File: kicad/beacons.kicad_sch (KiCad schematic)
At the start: 23 parts, among them J1 USB_C_Receptacle_USB2.0_16P, J2 Conn_01x03, J3 Conn_01x18, U1 ESP32-S3-WROOM-1, U2 PN5321A3HN_C1xx, U3 74HC595

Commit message: Fix
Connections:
- net +3V3: now also U1.3 (EN)
- net VCC: no longer U1.3 (EN)

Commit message: More pcb work
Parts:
- removed U1: ESP32-S3-WROOM-1, RF_Module:ESP32-S3-WROOM-1, symbol RF_Module:ESP32-S3-WROOM-1
- added AE1: Antenna_Loop, symbol Device:Antenna_Loop
- added C1, C14, C2, C5: 100nF, Capacitor_SMD:C_0402_1005Metric, symbol Device:C
- added C10, C11: NFC_C2, Capacitor_SMD:C_0402_1005Metric, symbol Device:C
- added C12: .1uF, Capacitor_SMD:C_0402_1005Metric, symbol Device:C
- added C13: 4.7uF, Capacitor_SMD:C_0402_1005Metric, symbol Device:C
- added C15, C17: 47uF, Capacitor_SMD:C_0402_1005Metric, symbol Device:C
- added C16: 10nF, Capacitor_SMD:C_0402_1005Metric, symbol Device:C
- added C3, C4: 22pF, Capacitor_SMD:C_0402_1005Metric, symbol Device:C
- added C6, C7: 220pF, Capacitor_SMD:C_0402_1005Metric, symbol Device:C
- added C8, C9: NFC_C1, Capacitor_SMD:C_0402_1005Metric, symbol Device:C
- added IC1: AP7179DSKZ20-13, QFN50P350X350X80-21N-D, symbol AP7179DSKZ20-13:AP7179DSKZ20-13
- added J4: Conn_01x02, Connector_JST:JST_PH_B2B-PH-K_1x02_P2.00mm_Vertical, symbol Connector_Generic:Conn_01x02
- added L1, L2: 560nH, Inductor_SMD:L_0603_1608Metric, symbol Device:L
- added Q1: Q_NPN, symbol Device:Q_NPN
- added R10: 2k, Resistor_SMD:R_0402_1005Metric, symbol Device:R
- added R11, R9: 10k, Resistor_SMD:R_0402_1005Metric, symbol Device:R
- added R5: 1k, Resistor_SMD:R_0402_1005Metric, symbol Device:R
- added R6: 2.7k, Resistor_SMD:R_0402_1005Metric, symbol Device:R
- added R7, R8: NFC_RQ, Resistor_SMD:R_0402_1005Metric, symbol Device:R
- added SW1: SW_Push, symbol Switch:SW_Push
- added SW2: SW_SPST, symbol Switch:SW_SPST
- added U1: ESP32-S3-WROOM-1, PCM_Espressif:ESP32-S3-WROOM-1, symbol PCM_Espressif:ESP32-S3-WROOM-1
- added U4: MAX17048G+T10, footprints:21-0168E_T822-3_MXM, symbol battmon:MAX17048G+T10
- added U5: MCP73831-2-OT, Package_TO_SOT_SMD:SOT-23-5, symbol Battery_Management:MCP73831-2-OT
- added Y1: Crystal 27.12MHz, symbol Device:Crystal
- D1: footprint (none) -> Diode_SMD:D_SOD-323
- J1: footprint (none) -> Connector_USB:USB_C_Receptacle_GCT_USB4105-xx-A_16P_TopMnt_Horizontal
- J2: footprint (none) -> Connector_JST:JST_PH_B3B-PH-K_1x03_P2.00mm_Vertical
- LED1, LED2: footprint SC10-11EWA_KNB -> footprints:SC10-11EWA_KNB
- R1, R2: value R -> 330; footprint (none) -> Resistor_SMD:R_0402_1005Metric
- R3, R4: footprint (none) -> Resistor_SMD:R_0402_1005Metric
- U3: footprint (none) -> Package_SO:SSOP-16_5.3x6.2mm_P0.65mm
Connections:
- net I2C_SDA is gone; now on net I2C_SCL: J3.14 (Pin_14)
- net +3V3: now also U2.17 (I1), U2.23 (PVDD), U2.39 (DVDD), U2.40 (VBAT), U2.5 (TVDD), U2.8 (AVDD), C1.2, C12.1, C2.2, R9.2, U1.2 (3V3), U1.3 (EN), U4.3 (VDD)
- net +5V: now also C14.2, C17.2, IC1.1 (OUT_1), Q1.C, U5.4 (V_{DD})
- net GND: now also U2.1 (DVSS), U2.11 (AVSS), U2.16 (I0), U2.18 (TESTEN), U2.3 (TVSS1), U2.41 (AVSS), U2.7 (TVSS2), C1.1, C10.2, C11.1, C12.2, C13.1, C14.1, C15.1, C16.1, C17.1, C2.1, C3.1, C4.2, C5.2, C6.1, C7.1, IC1.18 (GND_2), IC1.8 (GND_1), J4.2 (Pin_2), R10.1, SW1.2, U1.1 (GND), U1.16 (GPIO46), U1.40 (GND), U1.41 (GND), U4.1 (CTG), U4.4 (GND), U4.9 (EPAD), U5.2 (V_{SS})
- net I2C_SCL: now also U2.27 (NSS/P50_SCL/HSU_RX), U2.28 (MOSI/SDA/HSU_TX), U4.6 (QSTRT), U4.7 (SCL), U4.8 (SDA)
- net LED_SPI: now also R11.1; no longer D2.4 (DIN)
- net USB_NEG: now also U1.13 (GPIO19/U1RTS/ADC2_CH8/CLK_OUT2/USB_D-)
- net USB_POS: now also U1.14 (GPIO20/U1CTS/ADC2_CH9/CLK_OUT1/USB_D+)
- net at U2.10 (RX): now also R5.1, R6.1
- net at U2.14 (OSCIN): now also C3.2, Y1.1
- net at U2.15 (OSCOUT): now also C4.1, Y1.2
- net NFC_RESET: now reaches U2.38 (~{RSTPD})
- net at U2.4 (TX1): now also L1.1
- net at U2.6 (TX2): now also L2.1
- net at U2.9 (VMID): now also C5.1, R5.2
- new net: C16.2, IC1.13 (NR/SS)
- new net: R10.2, U5.5 (PROG)
- new net: Q1.B, R11.2
- new net: C7.2, C9.1, L2.2
- new net: C10.1, C9.2, R8.1
- new net: C6.2, C8.1, L1.2, R6.2
- new net: C11.2, C8.2, R7.1
- new net: AE1.1, R7.2
- new net: AE1.2, R8.2
- new net CELL_POS: C13.2, J4.1 (Pin_1), SW2.1 (A), U4.2 (CELL), U5.3 (V_{BAT})
- new net CHARGE_STAT: U5.1 (STAT)
- new net ESP_BOOT: R9.1, SW1.1, U1.27 (GPIO0/BOOT)
- new net LED_SPI_5V: D2.4 (DIN), Q1.E
- new net REG_POS: C15.2, IC1.14 (EN), IC1.15 (IN_1), SW2.2 (B)
- no-connect marks 8 -> 37
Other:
- moved on the sheet: D1, D10, D11, D2, D3, D4, D5, D6, D7, D8, D9, J1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

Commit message: Tons of stuff
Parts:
- removed U2: PN5321A3HN_C1xx, Package_DFN_QFN:HVQFN-40-1EP_6x6mm_P0.5mm_EP4.1x4.1mm, symbol RF_NFC:PN5321A3HN_C1xx
- added C18, C20: 10nF, symbol Device:C
- added C19, C21: 47uF, Capacitor_SMD:C_0402_1005Metric, symbol Device:C
- added C22: 10nF, Capacitor_SMD:C_0402_1005Metric, symbol Device:C
- added C23, C24: C_RX, symbol Device:C
- added C25, C27: C_0, symbol Device:C
- added C29, C31: C_1, symbol Device:C
- added C33, C34: C_2, symbol Device:C
- added IC2: AP7179DSKZ20-13, QFN50P350X350X80-21N-D, symbol AP7179DSKZ20-13:AP7179DSKZ20-13
- added IC3: PN7160A1HN_C100E, QFN50P600X600X100-41N-D, symbol PN7160A1HN_C100E:PN7160A1HN_C100E
- added R12: 12.4k, symbol Device:R
- added R13: 2.37k, symbol Device:R
- added R14: 11.8k, symbol Device:R
- added R15: 3.74k, symbol Device:R
- AE1: footprint (none) -> footprints:NFC
- C1: footprint Capacitor_SMD:C_0402_1005Metric -> (none)
- C10: value NFC_C2 -> 100nF; footprint Capacitor_SMD:C_0402_1005Metric -> (none)
- C11: value NFC_C2 -> 4.7uF; footprint Capacitor_SMD:C_0402_1005Metric -> (none)
- C3, C4: value 22pF -> 2.2uF; footprint Capacitor_SMD:C_0402_1005Metric -> (none)
- C5: value 100nF -> 22pF; footprint Capacitor_SMD:C_0402_1005Metric -> (none)
- C6: value 220pF -> 22pF; footprint Capacitor_SMD:C_0402_1005Metric -> (none)
- C7: value 220pF -> 2.2uF; footprint Capacitor_SMD:C_0402_1005Metric -> (none)
- C8: value NFC_C1 -> 2.2uF; footprint Capacitor_SMD:C_0402_1005Metric -> (none)
- C9: value NFC_C1 -> 4.7uF; footprint Capacitor_SMD:C_0402_1005Metric -> (none)
- L1, L2: value 560nH -> L_0; footprint Inductor_SMD:L_0603_1608Metric -> (none)
- R5: value 1k -> R_RX; footprint Resistor_SMD:R_0402_1005Metric -> (none)
- R6: value 2.7k -> R_RX; footprint Resistor_SMD:R_0402_1005Metric -> (none)
- R7, R8: value NFC_RQ -> R_Q; footprint Resistor_SMD:R_0402_1005Metric -> (none)
- SW2: footprint (none) -> Connector_JST:JST_PH_B2B-PH-K_1x02_P2.00mm_Vertical
- Y1: value Crystal 27.12MHz -> 27.12MHz Crystal
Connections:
- net +3V3: now also C19.2, C20.1, IC2.1 (OUT_1), IC3.10 (VEN), R14.2; no longer C1.2
- net +5V: now also C18.1, R12.2
- net GND: now also C1.2, C11.2, C3.2, C5.1, C7.2, C8.2, C9.2, C19.1, C21.1, C22.1, C25.2, C27.1, C33.2, C34.1, IC2.18 (GND_2), IC2.8 (GND_1), IC3.1 (I2C_ADR0/SPI_NSS), IC3.20 (VSS(TX)), IC3.3 (I2C_ADR1/SPI_MOSI), IC3.4 (VSS_1), IC3.41 (VSS_2), IC3.9 (VSS(A)), R13.2, R15.2; no longer C1.1, C11.1, C3.1, C5.2, C7.1
- net I2C_SCL: now also IC3.7 (I2C_SCL/SPI_SCK); no longer J3.14 (Pin_14), U4.6 (QSTRT), U4.8 (SDA)
- net NFC_IRQ: now also IC3.8 (IRQ)
- net REG_POS: now also C21.2, IC2.14 (EN), IC2.15 (IN_1)
- net at R6.1: now also C24.2; no longer R5.1
- net at R5.2: now also L1.2, C25.1, C29.1; no longer C5.1
- net at Y1.1: now also C6.2, IC3.29 (XTAL2); no longer C3.2
- net at Y1.2: now also C5.2, IC3.30 (NFC_CLK_XTAL1); no longer C4.1
- net NFC_TX1: now reaches L1.1
- net NFC_TX1: now also IC3.21 (TX1)
- net NFC_TX2: now reaches L2.1
- net NFC_TX2: now also IC3.19 (TX2)
- net at IC1.3 (FB): now also C18.2, R12.1, R13.1
- new net: C20.2, IC2.3 (FB), R14.1, R15.1
- new net: C29.2, C33.1, R7.1
- new net: C10.1, C9.1, IC3.12 (VBAT2), IC3.28 (VBAT)
- new net: C27.2, C31.1, L2.2, R6.2
- new net: C3.1, C4.1, IC3.14 (VDD(TX)), IC3.18 (TVDD_IN), IC3.22 (VDD_IN2)
- new net: C11.1, IC3.13 (VDD(UP))
- new net: C7.1, C8.1, IC3.26 (VDD(A)), IC3.27 (VDD_2), IC3.31 (VDD(D)), IC3.6 (VDD_1)
- new net: C22.2, IC2.13 (NR/SS)
- new net: C23.2, R5.1
- new net: C31.2, C34.2, R8.1
- new net: C1.1, IC3.17 (VDD(VMID))
- new net I2C_SDA: IC3.5 (I2C_SDA/SPI_MISO), J3.14 (Pin_14), U4.8 (SDA)
- new net NFC_FWUD: IC3.2 (DWL_REQ)
- new net NFC_RXN: C24.1, IC3.15 (RXN)
- new net NFC_RXP: C23.1, IC3.16 (RXP)
- no-connect marks 37 -> 48
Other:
- moved on the sheet: C17, J3

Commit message: Routing and RF
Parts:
- removed AE1: Antenna_Loop, footprints:NFC, symbol Device:Antenna_Loop
- removed C1, C10: 100nF, symbol Device:C
- removed C11, C9: 4.7uF, symbol Device:C
- removed C23, C24: C_RX, symbol Device:C
- removed C25, C27: C_0, symbol Device:C
- removed C29, C31: C_1, symbol Device:C
- removed C3, C4, C7, C8: 2.2uF, symbol Device:C
- removed C33, C34: C_2, symbol Device:C
- removed C5, C6: 22pF, symbol Device:C
- removed D10, D11: WS2812B, LED_SMD:LED_WS2812B_PLCC4_5.0x5.0mm_P3.2mm, symbol LED:WS2812B
- removed IC3: PN7160A1HN_C100E, QFN50P600X600X100-41N-D, symbol PN7160A1HN_C100E:PN7160A1HN_C100E
- removed L1, L2: L_0, symbol Device:L
- removed R5, R6: R_RX, symbol Device:R
- removed R7, R8: R_Q, symbol Device:R
- removed Y1: 27.12MHz Crystal, symbol Device:Crystal
- C18, C20: footprint (none) -> Capacitor_SMD:C_0402_1005Metric
- IC1, IC2: footprint QFN50P350X350X80-21N-D -> footprints:QFN50P350X350X80-21N-D
- J4, SW2: footprint Connector_JST:JST_PH_B2B-PH-K_1x02_P2.00mm_Vertical -> Connector_AMASS:AMASS_XT30UPB-M_1x02_P5.0mm_Vertical
- Q1: footprint (none) -> Package_TO_SOT_SMD:SOT-23; symbol Device:Q_NPN -> Transistor_BJT:MMBT3904
- R12, R13, R14, R15: footprint (none) -> Resistor_SMD:R_0402_1005Metric
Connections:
- net VCC is gone; now on net +3V3: U3.10 (~{SRCLR})
- net +5V: now also Q1.3 (C); no longer C14.2, D1.1 (K), Q1.C, U5.4 (V_{DD})
- net GND: now also U4.6 (QSTRT)
- net LED_PEAK: now also D9.2 (DOUT)
- net LED_SPI_5V: now also Q1.2 (E); no longer Q1.E
- net at R11.2: now also Q1.1 (B); no longer Q1.B
- net at LED2.14: now also LED2.3, LED2.6, R2.1
- net at LED1.6, R1.1: now also LED1.14, LED1.3
- new net USB_VBUS: C14.2, D1.1 (K), U5.4 (V_{DD})
- no-connect marks 48 -> 38
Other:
- added sheet NFC (nfc.kicad_sch)
- moved on the sheet: D1, J1, J3, LED1, LED2, R1, R11, R2, R3, R4, U3

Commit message: First revision
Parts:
- added C28, C30: .1uF, Capacitor_SMD:C_0402_1005Metric, symbol Device:C
- added C32: 22uF, Capacitor_SMD:C_0402_1005Metric, symbol Device:C
- added SW2: SW_Push, footprints:SMT_4.2X3.2_, symbol SKRPACE010:SKRPACE010
- J3: footprint (none) -> footprints:DisplayConnector
- SW1: footprint (none) -> footprints:SMT_4.2X3.2_; symbol Switch:SW_Push -> SKRPACE010:SKRPACE010; Arrow Part Number (none) -> SKRPACE010; Arrow Price/Stock (none) -> https://www.arrow.com/en/products/skrpace010/alps-electric; Manufacturer_Name (none) -> ALPS Electric; Manufacturer_Part_Number (none) -> SKRPACE010; Mouser Part Number (none) -> 688-SKRPACE010; Mouser Price/Stock (none) -> https://www.mouser.co.uk/ProductDetail/Alps-Alpine/SKRPACE0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
- renumbered SW2 to SW3
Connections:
- net +3V3: now also R9.1, C32.2; no longer R9.2, U1.3 (EN)
- net CHARGE_STAT: now also U1.12 (GPIO8/TOUCH8/ADC1_CH7/SUBSPICS1)
- net DISP_CS: now also U1.36 (U0RXD/GPIO44/CLK_OUT2)
- net DISP_RESET: now also U1.21 (GPIO13/TOUCH13/ADC2_CH2/FSPIQ/FSPIIO7/SUBSPIQ)
- net ESP_BOOT: now also SW1.2, C28.1; no longer R9.1
- net GND: now also SW1.3, SW1.4, C28.2, C30.2, C32.1, SW2.3, SW2.4; no longer SW1.2
- net I2C_SCL: now also U1.19 (GPIO11/TOUCH11/ADC2_CH0/FSPID/FSPIIO5/SUBSPID)
- net I2C_SDA: now also U1.18 (GPIO10/TOUCH10/ADC1_CH9/FSPICS0/FSPIIO4/SUBSPICS0)
- net LED_SPI: now also U1.37 (U0TXD/GPIO43/CLK_OUT1)
- net NFC_FWUD: now also U1.15 (GPIO3/TOUCH3/ADC1_CH2)
- net NFC_IRQ: now also U1.11 (GPIO18/U1RXD/ADC2_CH7/CLK_OUT3)
- net SPI_CLK: now also U1.26 (GPIO45)
- net SPI_DATA0: now also U1.25 (GPIO48/SPICLK_N/SUBSPICLK_N_DIFF)
- net SPI_DATA1: now also U1.24 (GPIO47/SPICLK_P/SUBSPICLK_P_DIFF)
- net SPI_DATA2: now also U1.23 (GPIO21)
- net SPI_DATA3: now also U1.22 (GPIO14/TOUCH14/ADC2_CH3/FSPIWP/FSPIDQS/SUBSPIWP)
- net SR_CS: now also U1.4 (GPIO4/TOUCH4/ADC1_CH3)
- net SS0: now also U1.9 (GPIO16/U0CTS/ADC2_CH5/XTAL_32K_N)
- net SS1: now also U1.10 (GPIO17/U1TXD/ADC2_CH6)
- net TOUCH_IRQ: now also U1.17 (GPIO9/TOUCH9/ADC1_CH8/FSPIHD/SUBSPIHD)
- net TOUCH_RESET: now also U1.20 (GPIO12/TOUCH12/ADC2_CH1/FSPICLK/FSPIIO6/SUBSPICLK)
- new net ESP_EN: C30.1, R9.2, SW2.1, SW2.2, U1.3 (EN)
- no-connect marks 38 -> 45

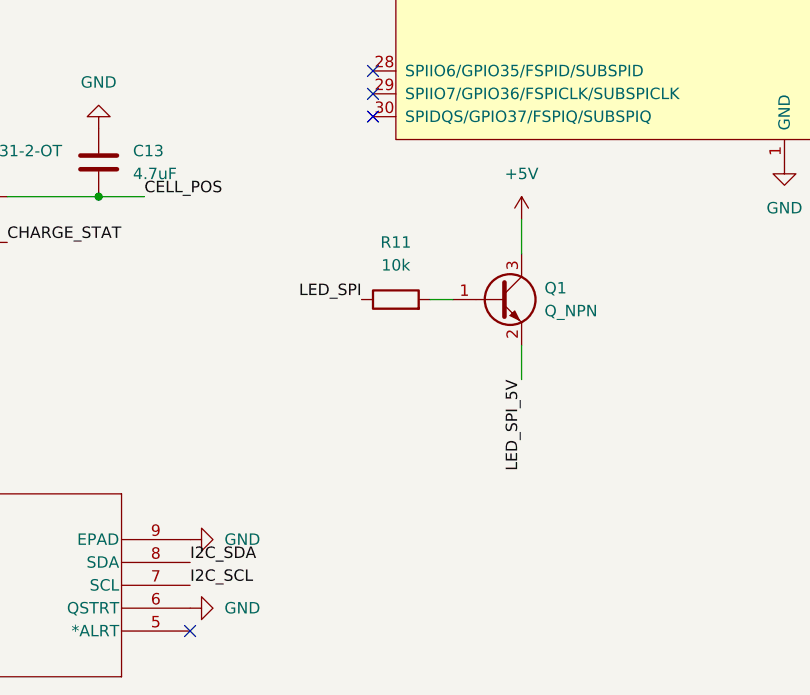
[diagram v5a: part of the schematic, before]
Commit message: Added level shifter
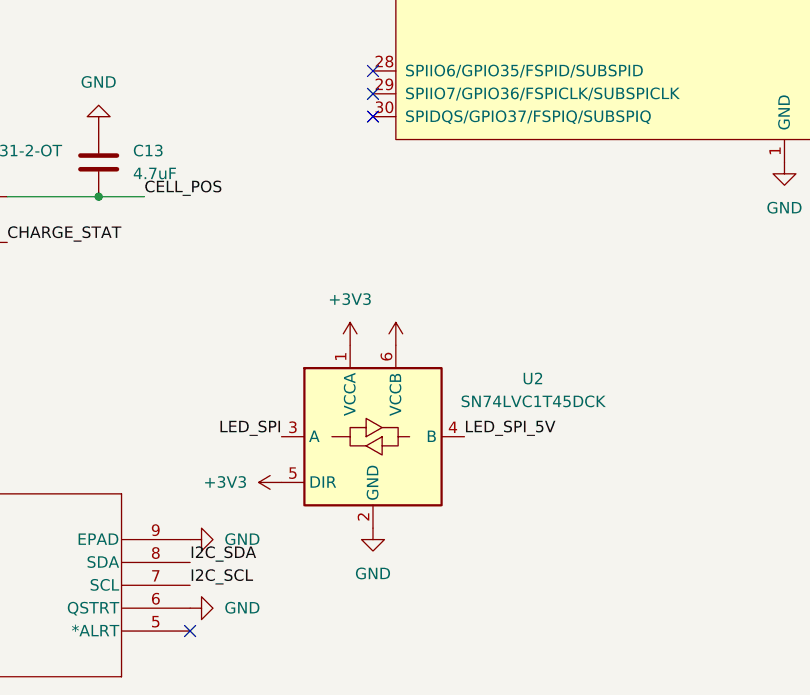
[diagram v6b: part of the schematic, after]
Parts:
- removed Q1: Q_NPN, Package_TO_SOT_SMD:SOT-23, symbol Transistor_BJT:MMBT3904
- removed R11: 10k, Resistor_SMD:R_0402_1005Metric, symbol Device:R
- added U2: SN74LVC1T45DCK, Package_TO_SOT_SMD:SOT-363_SC-70-6, symbol Logic_LevelTranslator:SN74LVC1T45DCK
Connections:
- net +3V3: now also U2.1 (VCCA), U2.5 (DIR)
- net +5V: now also U2.6 (VCCB)
- net GND: now also U2.2 (GND)
- net LED_SPI: now also U2.3 (A)
- net LED_SPI_5V: now also U2.4 (B)
